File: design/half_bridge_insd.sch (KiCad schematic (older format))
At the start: 13 parts

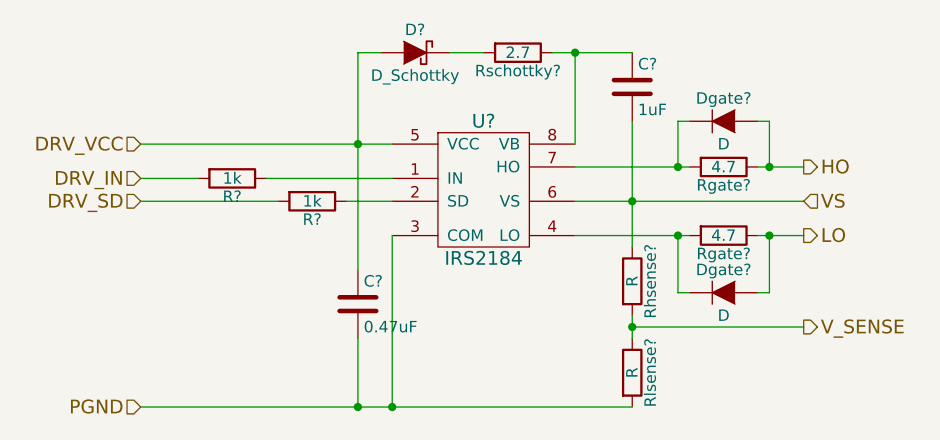
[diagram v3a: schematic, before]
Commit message: Assigned some footprints.
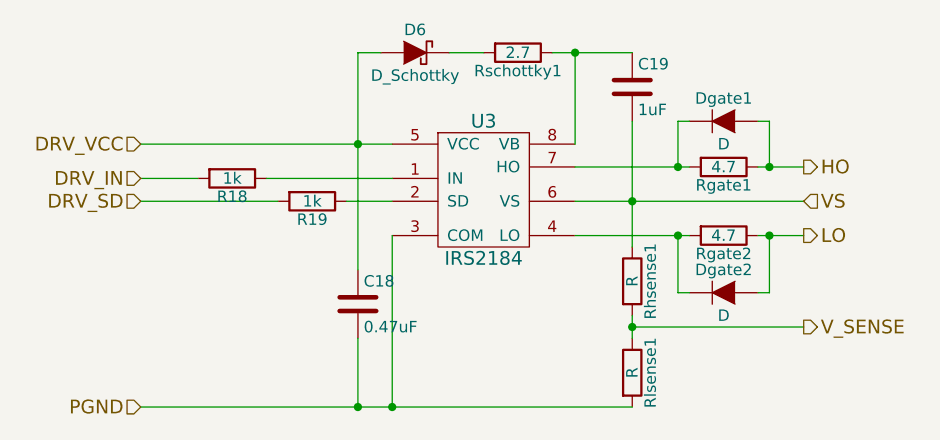
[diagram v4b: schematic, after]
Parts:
- C18: renamed from C?; footprint (none) -> Capacitors_SMD:C_0805_HandSoldering
- C19: renamed from C?; footprint (none) -> Capacitors_SMD:C_1210_HandSoldering
- D6: renamed from D?; footprint (none) -> Diodes_SMD:DO-214AB
- Dgate1, Dgate2: renamed from Dgate?; footprint (none) -> Diodes_SMD:SOD-123
- gave numbers to parts that had none: 8
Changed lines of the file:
@@
 $EndDescr
 $Comp
-L IRS2184 U?
+L IRS2184 U3
 U 1 1 55DDD5BF
 P 5450 3400
-AR Path="/55DB7E47/55DDD5BF" Ref="U?"  Part="1"
+AR Path="/55DB7E47/55DDD5BF" Ref="U3"  Part="1"
 AR Path="/55E59DEF/55DDD5BF" Ref="U?"  Part="1"
-AR Path="/55E6829E/55DDD5BF" Ref="U?"  Part="1"
-AR Path="/55E631D7/55DDD5BF" Ref="U?"  Part="1"
-F 0 "U?" H 5450 3700 60  0000 C CNN
+AR Path="/55E6829E/55DDD5BF" Ref="U5"  Part="1"
+AR Path="/55E631D7/55DDD5BF" Ref="U4"  Part="1"
+F 0 "U3" H 5450 3700 60  0000 C CNN
 F 1 "IRS2184" H 5450 3100 60  0000 C CNN
-F 2 "" H 5450 3400 60  0000 C CNN
+F 2 "" H 5450 3400 60  0001 C CNN
 F 3 "" H 5450 3400 60  0000 C CNN
 	1    5450 3400
@@
 PGND
 $Comp
-L D_Schottky D?
+L D_Schottky D6
 U 1 1 55DE445F
 P 5150 2800
-AR Path="/55DB7E47/55DE445F" Ref="D?"  Part="1"
+AR Path="/55DB7E47/55DE445F" Ref="D6"  Part="1"
 AR Path="/55E59DEF/55DE445F" Ref="D?"  Part="1"
-AR Path="/55E6829E/55DE445F" Ref="D?"  Part="1"
-AR Path="/55E631D7/55DE445F" Ref="D?"  Part="1"
-F 0 "D?" H 5150 2900 50  0000 C CNN
+AR Path="/55E6829E/55DE445F" Ref="D8"  Part="1"
+AR Path="/55E631D7/55DE445F" Ref="D7"  Part="1"
+F 0 "D6" H 5150 2900 50  0000 C CNN
 F 1 "D_Schottky" H 5150 2700 50  0000 C CNN
-F 2 "" H 5150 2800 60  0000 C CNN
+F 2 "Diodes_SMD:DO-214AB" H 5150 2800 60  0001 C CNN
 F 3 "" H 5150 2800 60  0000 C CNN
 	1    5150 2800
@@
 $EndComp
 $Comp
-L R R?
+L R R18
 U 1 1 55DF8324
 P 4350 3350
-AR Path="/55DB7E47/55DF8324" Ref="R?"  Part="1"
+AR Path="/55DB7E47/55DF8324" Ref="R18"  Part="1"
 AR Path="/55E59DEF/55DF8324" Ref="R?"  Part="1"
-AR Path="/55E6829E/55DF8324" Ref="R?"  Part="1"
-AR Path="/55E631D7/55DF8324" Ref="R?"  Part="1"
-F 0 "R?" V 4430 3350 50  0000 C CNN
+AR Path="/55E6829E/55DF8324" Ref="R23"  Part="1"
+AR Path="/55E631D7/55DF8324" Ref="R20"  Part="1"
+F 0 "R18" V 4430 3350 50  0000 C CNN
 F 1 "1k" V 4350 3350 50  0000 C CNN
-F 2 "" V 4280 3350 30  0000 C CNN
+F 2 "" V 4280 3350 30  0001 C CNN
 F 3 "" H 4350 3350 30  0000 C CNN
 	1    4350 3350
@@
 $EndComp
 $Comp
-L R Rschottky?
+L R Rschottky1
 U 1 1 55DF8357
 P 5600 2800
-AR Path="/55DB7E47/55DF8357" Ref="Rschottky?"  Part="1"
+AR Path="/55DB7E47/55DF8357" Ref="Rschottky1"  Part="1"
 AR Path="/55E59DEF/55DF8357" Ref="Rschottky?"  Part="1"
-AR Path="/55E6829E/55DF8357" Ref="Rschottky?"  Part="1"
-AR Path="/55E631D7/55DF8357" Ref="Rschottky?"  Part="1"
-F 0 "Rschottky?" V 5680 2800 50  0000 C CNN
+AR Path="/55E6829E/55DF8357" Ref="Rschottky3"  Part="1"
+AR Path="/55E631D7/55DF8357" Ref="Rschottky2"  Part="1"
+F 0 "Rschottky1" V 5680 2800 50  0000 C CNN
 F 1 "2.7" V 5600 2800 50  0000 C CNN
-F 2 "" V 5530 2800 30  0000 C CNN
+F 2 "" V 5530 2800 30  0001 C CNN
 F 3 "" H 5600 2800 30  0000 C CNN
 	1    5600 2800
@@
 $EndComp
 $Comp
-L R R?
+L R R19
 U 1 1 55DF8392
 P 4700 3450
-AR Path="/55DB7E47/55DF8392" Ref="R?"  Part="1"
+AR Path="/55DB7E47/55DF8392" Ref="R19"  Part="1"
 AR Path="/55E59DEF/55DF8392" Ref="R?"  Part="1"
-AR Path="/55E6829E/55DF8392" Ref="R?"  Part="1"
-AR Path="/55E631D7/55DF8392" Ref="R?"  Part="1"
-F 0 "R?" V 4780 3450 50  0000 C CNN
+AR Path="/55E6829E/55DF8392" Ref="R24"  Part="1"
+AR Path="/55E631D7/55DF8392" Ref="R21"  Part="1"
+F 0 "R19" V 4780 3450 50  0000 C CNN
 F 1 "1k" V 4700 3450 50  0000 C CNN
-F 2 "" V 4630 3450 30  0000 C CNN
+F 2 "" V 4630 3450 30  0001 C CNN
 F 3 "" H 4700 3450 30  0000 C CNN
 	1    4700 3450
@@
 $EndComp
 $Comp
-L R Rgate?
+L R Rgate1
 U 1 1 55DF83B9
 P 6500 3300
-AR Path="/55DB7E47/55DF83B9" Ref="Rgate?"  Part="1"
+AR Path="/55DB7E47/55DF83B9" Ref="Rgate1"  Part="1"
 AR Path="/55E59DEF/55DF83B9" Ref="Rgate?"  Part="1"
-AR Path="/55E6829E/55DF83B9" Ref="Rgate?"  Part="1"
-AR Path="/55E631D7/55DF83B9" Ref="Rgate?"  Part="1"
-F 0 "Rgate?" V 6580 3300 50  0000 C CNN
+AR Path="/55E6829E/55DF83B9" Ref="Rgate5"  Part="1"
+AR Path="/55E631D7/55DF83B9" Ref="Rgate3"  Part="1"
+F 0 "Rgate1" V 6580 3300 50  0000 C CNN
 F 1 "4.7" V 6500 3300 50  0000 C CNN
-F 2 "" V 6430 3300 30  0000 C CNN
+F 2 "" V 6430 3300 30  0001 C CNN
 F 3 "" H 6500 3300 30  0000 C CNN
 	1    6500 3300
@@
 $EndComp
 $Comp
-L R Rgate?
+L R Rgate2
 U 1 1 55DF843E
 P 6500 3600
-AR Path="/55DB7E47/55DF843E" Ref="Rgate?"  Part="1"
+AR Path="/55DB7E47/55DF843E" Ref="Rgate2"  Part="1"
 AR Path="/55E59DEF/55DF843E" Ref="Rgate?"  Part="1"
-AR Path="/55E6829E/55DF843E" Ref="Rgate?"  Part="1"
-AR Path="/55E631D7/55DF843E" Ref="Rgate?"  Part="1"
-F 0 "Rgate?" V 6580 3600 50  0000 C CNN
+AR Path="/55E6829E/55DF843E" Ref="Rgate6"  Part="1"
+AR Path="/55E631D7/55DF843E" Ref="Rgate4"  Part="1"
+F 0 "Rgate2" V 6580 3600 50  0000 C CNN
 F 1 "4.7" V 6500 3600 50  0000 C CNN
-F 2 "" V 6430 3600 30  0000 C CNN
+F 2 "" V 6430 3600 30  0001 C CNN
 F 3 "" H 6500 3600 30  0000 C CNN
 	1    6500 3600
@@
 	3950 3450 4550 3450
 $Comp
-L C C?
+L C C19
 U 1 1 55DF8D4F
 P 6100 2950
-AR Path="/55DB7E47/55DF8D4F" Ref="C?"  Part="1"
+AR Path="/55DB7E47/55DF8D4F" Ref="C19"  Part="1"
 AR Path="/55E59DEF/55DF8D4F" Ref="C?"  Part="1"
-AR Path="/55E6829E/55DF8D4F" Ref="C?"  Part="1"
-AR Path="/55E631D7/55DF8D4F" Ref="C?"  Part="1"
-F 0 "C?" H 6125 3050 50  0000 L CNN
+AR Path="/55E6829E/55DF8D4F" Ref="C23"  Part="1"
+AR Path="/55E631D7/55DF8D4F" Ref="C21"  Part="1"
+F 0 "C19" H 6125 3050 50  0000 L CNN
 F 1 "1uF" H 6125 2850 50  0000 L CNN
-F 2 "" H 6138 2800 30  0000 C CNN
+F 2 "Capacitors_SMD:C_1210_HandSoldering" H 6138 2800 30  0001 C CNN
 F 3 "" H 6100 2950 60  0000 C CNN
 	1    6100 2950
@@
 $EndComp
 $Comp
-L C C?
+L C C18
 U 1 1 55DF8D84
 P 4900 3900
-AR Path="/55DB7E47/55DF8D84" Ref="C?"  Part="1"
+AR Path="/55DB7E47/55DF8D84" Ref="C18"  Part="1"
 AR Path="/55E59DEF/55DF8D84" Ref="C?"  Part="1"
-AR Path="/55E6829E/55DF8D84" Ref="C?"  Part="1"
-AR Path="/55E631D7/55DF8D84" Ref="C?"  Part="1"
-F 0 "C?" H 4925 4000 50  0000 L CNN
+AR Path="/55E6829E/55DF8D84" Ref="C22"  Part="1"
+AR Path="/55E631D7/55DF8D84" Ref="C20"  Part="1"
+F 0 "C18" H 4925 4000 50  0000 L CNN
 F 1 "0.47uF" H 4925 3800 50  0000 L CNN
-F 2 "" H 4938 3750 30  0000 C CNN
+F 2 "Capacitors_SMD:C_0805_HandSoldering" H 4938 3750 30  0001 C CNN
 F 3 "" H 4900 3900 60  0000 C CNN
 	1    4900 3900
@@
 V_SENSE
 $Comp
-L R Rhsense?
+L R Rhsense1
 U 1 1 55E0598B
 P 6100 3800
-AR Path="/55DB7E47/55E0598B" Ref="Rhsense?"  Part="1"
+AR Path="/55DB7E47/55E0598B" Ref="Rhsense1"  Part="1"
 AR Path="/55E59DEF/55E0598B" Ref="Rhsense?"  Part="1"
-AR Path="/55E6829E/55E0598B" Ref="Rhsense?"  Part="1"
-AR Path="/55E631D7/55E0598B" Ref="Rhsense?"  Part="1"
-F 0 "Rhsense?" V 6180 3800 50  0000 C CNN
+AR Path="/55E6829E/55E0598B" Ref="Rhsense3"  Part="1"
+AR Path="/55E631D7/55E0598B" Ref="Rhsense2"  Part="1"
+F 0 "Rhsense1" V 6180 3800 50  0000 C CNN
 F 1 "R" V 6100 3800 50  0000 C CNN
-F 2 "" V 6030 3800 30  0000 C CNN
+F 2 "" V 6030 3800 30  0001 C CNN
 F 3 "" H 6100 3800 30  0000 C CNN
 	1    6100 3800
@@
 $EndComp
 $Comp
-L R Rlsense?
+L R Rlsense1
 U 1 1 55E05BEF
 P 6100 4200
-AR Path="/55DB7E47/55E05BEF" Ref="Rlsense?"  Part="1"
+AR Path="/55DB7E47/55E05BEF" Ref="Rlsense1"  Part="1"
 AR Path="/55E59DEF/55E05BEF" Ref="Rlsense?"  Part="1"
-AR Path="/55E6829E/55E05BEF" Ref="Rlsense?"  Part="1"
-AR Path="/55E631D7/55E05BEF" Ref="Rlsense?"  Part="1"
-F 0 "Rlsense?" V 6180 4200 50  0000 C CNN
+AR Path="/55E6829E/55E05BEF" Ref="Rlsense3"  Part="1"
+AR Path="/55E631D7/55E05BEF" Ref="Rlsense2"  Part="1"
+F 0 "Rlsense1" V 6180 4200 50  0000 C CNN
 F 1 "R" V 6100 4200 50  0000 C CNN
-F 2 "" V 6030 4200 30  0000 C CNN
+F 2 "" V 6030 4200 30  0001 C CNN
 F 3 "" H 6100 4200 30  0000 C CNN
 	1    6100 4200
@@
 Connection ~ 6100 4000
 $Comp
-L D Dgate?
+L D Dgate1
 U 1 1 55E9685F
 P 6500 3100
-F 0 "Dgate?" H 6500 3200 50  0000 C CNN
+AR Path="/55DB7E47/55E9685F" Ref="Dgate1"  Part="1"
+AR Path="/55E631D7/55E9685F" Ref="Dgate3"  Part="1"
+AR Path="/55E6829E/55E9685F" Ref="Dgate5"  Part="1"
+F 0 "Dgate1" H 6500 3200 50  0000 C CNN
 F 1 "D" H 6500 3000 50  0000 C CNN
-F 2 "" H 6500 3100 60  0000 C CNN
+F 2 "Diodes_SMD:SOD-123" H 6500 3100 60  0001 C CNN
 F 3 "" H 6500 3100 60  0000 C CNN
 	1    6500 3100
@@
 Connection ~ 6300 3300
 $Comp
-L D Dgate?
+L D Dgate2
 U 1 1 55E96991
 P 6500 3850
-F 0 "Dgate?" H 6500 3950 50  0000 C CNN
+AR Path="/55DB7E47/55E96991" Ref="Dgate2"  Part="1"
+AR Path="/55E631D7/55E96991" Ref="Dgate4"  Part="1"
+AR Path="/55E6829E/55E96991" Ref="Dgate6"  Part="1"
+F 0 "Dgate2" H 6500 3950 50  0000 C CNN
 F 1 "D" H 6500 3750 50  0000 C CNN
-F 2 "" H 6500 3850 60  0000 C CNN
+F 2 "Diodes_SMD:SOD-123" H 6500 3850 60  0001 C CNN
 F 3 "" H 6500 3850 60  0000 C CNN
 	1    6500 3850

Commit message: Added footprint that fits SOD-123 and DO-214AC bootstrap diodes.
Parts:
- D6: footprint Diodes_SMD:DO-214AB -> FootprintsBLDC:DO-214AC_SOD-123
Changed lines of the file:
@@
 F 0 "D6" H 5150 2900 50  0000 C CNN
 F 1 "D_Schottky" H 5150 2700 50  0000 C CNN
-F 2 "Diodes_SMD:DO-214AB" H 5150 2800 60  0001 C CNN
+F 2 "FootprintsBLDC:DO-214AC_SOD-123" H 5150 2800 60  0001 C CNN
 F 3 "" H 5150 2800 60  0000 C CNN
 	1    5150 2800

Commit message: Selected footprints
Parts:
- R18, R19: footprint (none) -> Resistors_SMD:R_0603
- Rgate1, Rgate2, Rhsense1, Rschottky1: footprint (none) -> Resistors_SMD:R_0805_HandSoldering
- Rlsense1: footprint (none) -> Resistors_SMD:R_0603_HandSoldering
- U3: footprint (none) -> Housings_SOIC:SOIC-8_3.9x4.9mm_Pitch1.27mm
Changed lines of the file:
@@
 F 0 "U3" H 5450 3700 60  0000 C CNN
 F 1 "IRS2184" H 5450 3100 60  0000 C CNN
-F 2 "" H 5450 3400 60  0001 C CNN
+F 2 "Housings_SOIC:SOIC-8_3.9x4.9mm_Pitch1.27mm" H 5450 3400 60  0001 C CNN
 F 3 "" H 5450 3400 60  0000 C CNN
 	1    5450 3400
@@
 F 0 "R18" V 4430 3350 50  0000 C CNN
 F 1 "1k" V 4350 3350 50  0000 C CNN
-F 2 "" V 4280 3350 30  0001 C CNN
+F 2 "Resistors_SMD:R_0603" V 4280 3350 30  0001 C CNN
 F 3 "" H 4350 3350 30  0000 C CNN
 	1    4350 3350
@@
 F 0 "Rschottky1" V 5680 2800 50  0000 C CNN
 F 1 "2.7" V 5600 2800 50  0000 C CNN
-F 2 "" V 5530 2800 30  0001 C CNN
+F 2 "Resistors_SMD:R_0805_HandSoldering" V 5530 2800 30  0001 C CNN
 F 3 "" H 5600 2800 30  0000 C CNN
 	1    5600 2800
@@
 F 0 "R19" V 4780 3450 50  0000 C CNN
 F 1 "1k" V 4700 3450 50  0000 C CNN
-F 2 "" V 4630 3450 30  0001 C CNN
+F 2 "Resistors_SMD:R_0603" V 4630 3450 30  0001 C CNN
 F 3 "" H 4700 3450 30  0000 C CNN
 	1    4700 3450
@@
 F 0 "Rgate1" V 6580 3300 50  0000 C CNN
 F 1 "4.7" V 6500 3300 50  0000 C CNN
-F 2 "" V 6430 3300 30  0001 C CNN
+F 2 "Resistors_SMD:R_0805_HandSoldering" V 6430 3300 30  0001 C CNN
 F 3 "" H 6500 3300 30  0000 C CNN
 	1    6500 3300
@@
 F 0 "Rgate2" V 6580 3600 50  0000 C CNN
 F 1 "4.7" V 6500 3600 50  0000 C CNN
-F 2 "" V 6430 3600 30  0001 C CNN
+F 2 "Resistors_SMD:R_0805_HandSoldering" V 6430 3600 30  0001 C CNN
 F 3 "" H 6500 3600 30  0000 C CNN
 	1    6500 3600
@@
 F 0 "Rhsense1" V 6180 3800 50  0000 C CNN
 F 1 "R" V 6100 3800 50  0000 C CNN
-F 2 "" V 6030 3800 30  0001 C CNN
+F 2 "Resistors_SMD:R_0805_HandSoldering" V 6030 3800 30  0001 C CNN
 F 3 "" H 6100 3800 30  0000 C CNN
 	1    6100 3800
@@
 F 0 "Rlsense1" V 6180 4200 50  0000 C CNN
 F 1 "R" V 6100 4200 50  0000 C CNN
-F 2 "" V 6030 4200 30  0001 C CNN
+F 2 "Resistors_SMD:R_0603_HandSoldering" V 6030 4200 30  0001 C CNN
 F 3 "" H 6100 4200 30  0000 C CNN
 	1    6100 4200
